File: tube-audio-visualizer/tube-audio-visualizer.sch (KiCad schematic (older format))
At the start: 19 parts, among them T1 EM80, U1 LM741, U2 LM386

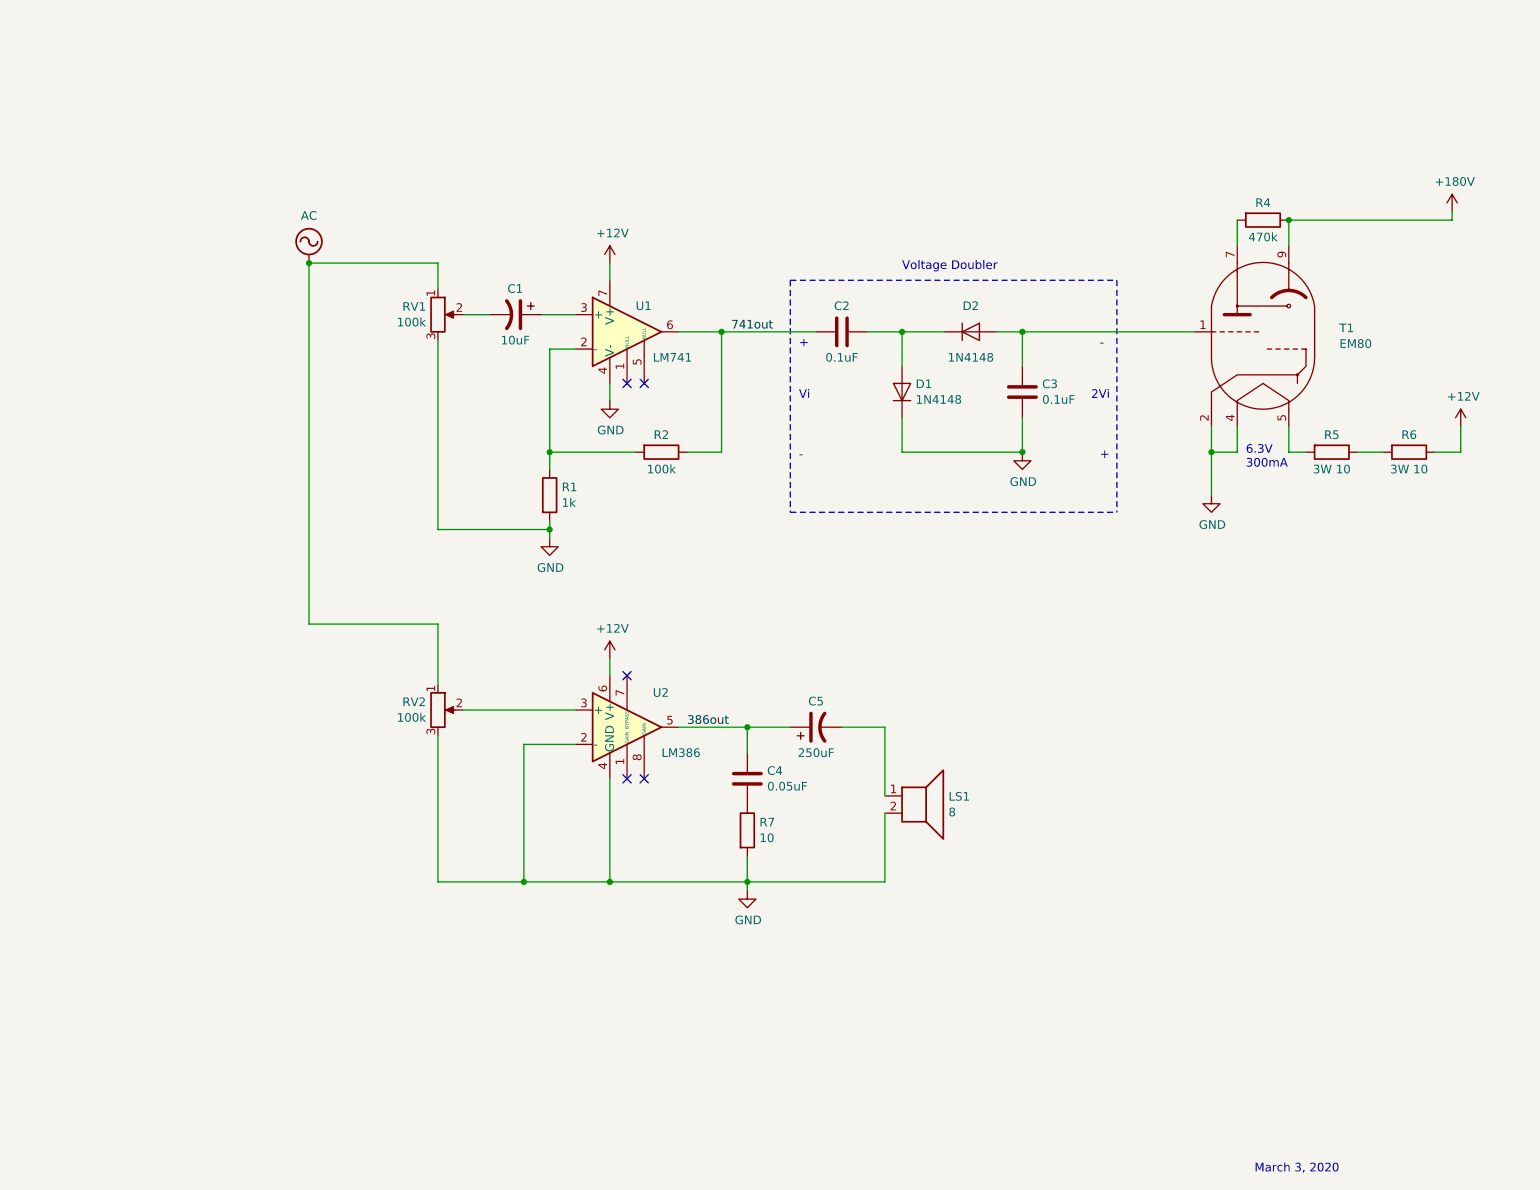
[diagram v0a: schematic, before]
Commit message: Added barrel jack to schematic. Connected 3.5mm female connector. Created footprint for 3.5mm female connector. Added footprints to all schematic symbols.
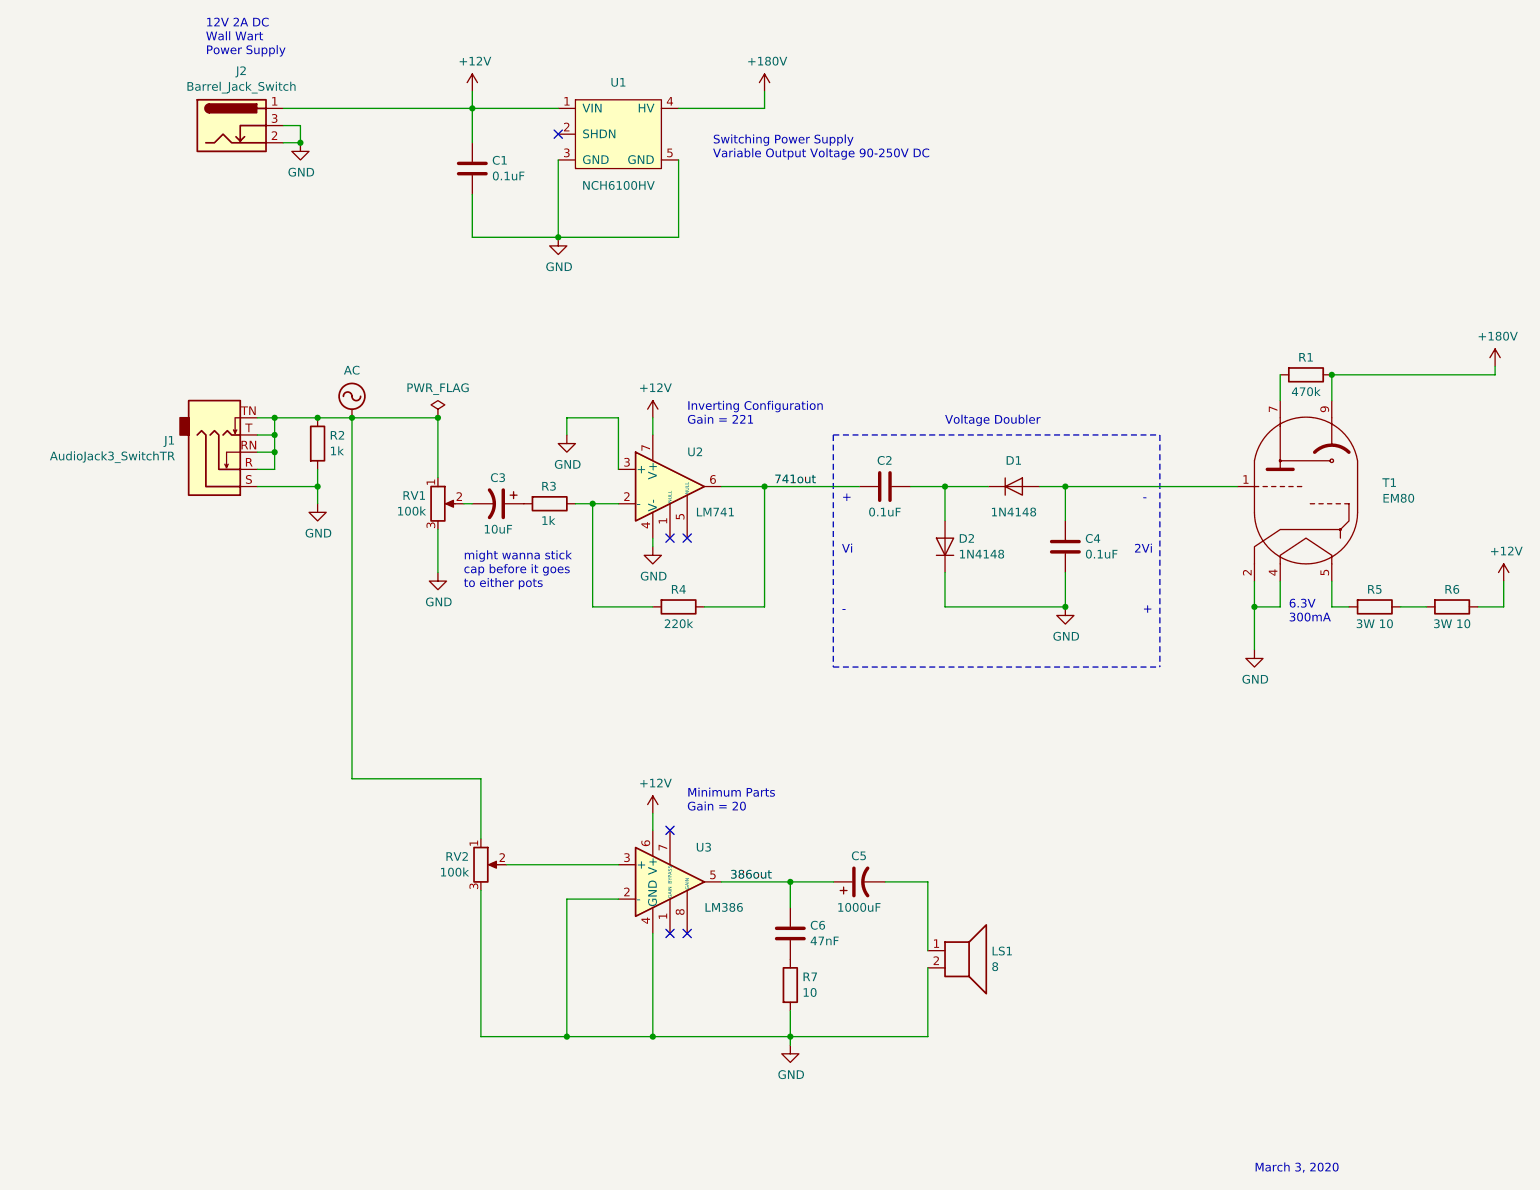
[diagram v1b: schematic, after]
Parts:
- added C1: 0.1uF, Capacitor_THT:C_Disc_D5.0mm_W2.5mm_P5.00mm, symbol Device:C
- added J1: AudioJack3_SwitchTR, footprints-nad:AudioJack_3_5_mm_Female, symbol Connector:AudioJack3_SwitchTR
- added J2: Barrel_Jack_Switch, Connector_BarrelJack:BarrelJack_CUI_PJ-102AH_Horizontal, symbol Connector:Barrel_Jack_Switch
- added R2: 1k, Resistor_THT:R_Axial_DIN0207_L6.3mm_D2.5mm_P10.16mm_Horizontal, symbol Device:R
- added U1: NCH6100HV, footprints-nad:NCH6100HV_PinSockets, symbol tube-audio-visualizer-rescue:NCH6100HV-symbols-nad
- C2: footprint (none) -> Capacitor_THT:C_Disc_D5.0mm_W2.5mm_P5.00mm
- C3: renamed from C1; footprint (none) -> Capacitor_THT:CP_Radial_D5.0mm_P2.00mm
- C4: renamed from C3; footprint (none) -> Capacitor_THT:C_Disc_D5.0mm_W2.5mm_P5.00mm
- C5: value 250uF -> 1000uF; footprint (none) -> Capacitor_THT:CP_Radial_D8.0mm_P3.50mm
- C6: renamed from C4; value 0.05uF -> 47nF; footprint (none) -> Capacitor_THT:C_Disc_D3.0mm_W2.0mm_P2.50mm
- D1: renamed from D2; footprint (none) -> Diode_THT:D_DO-35_SOD27_P7.62mm_Horizontal
- D2: renamed from D1; footprint (none) -> Diode_THT:D_DO-35_SOD27_P7.62mm_Horizontal
- LS1: footprint (none) -> Connector_PinSocket_2.54mm:PinSocket_1x02_P2.54mm_Vertical
- R4: renamed from R2; value 100k -> 220k
- R5, R6: footprint (none) -> Resistor_THT:R_Axial_DIN0516_L15.5mm_D5.0mm_P20.32mm_Horizontal
- RV1, RV2: footprint (none) -> Potentiometer_THT:Potentiometer_Bourns_3386P_Vertical
- renumbered R4 to R1, R1 to R3, U1 to U2, U2 to U3
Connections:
- net +12V: now also C1.1, J2.1, U1.1 (VIN)
- net +180V: now also U1.4 (HV)
- net AC: now also J1.R, J1.RN, J1.T, J1.TN, R2.1
- net GND: now also U2.3 (+), C1.2, J1.S, J2.2, J2.3, R2.2, U1.3 (GND), U1.5 (GND); no longer R3.2
- net at C3.1: now also R3.2; no longer U2.3 (+)
- no-connect marks 5 -> 6
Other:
- note added: "12V 2A DC\nWall Wart \nPower Supply"
- note added: "Inverting Configuration\nGain = 221"
- note added: "Minimum Parts\nGain = 20"
- note added: "Switching Power Supply\nVariable Output Voltage 90-250V DC"
- note added: "might wanna stick \ncap before it goes \nto either pots"
- moved on the sheet: C2, C3, C4, C5, C6, D1, D2, LS1, R1, R3, R4, R5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

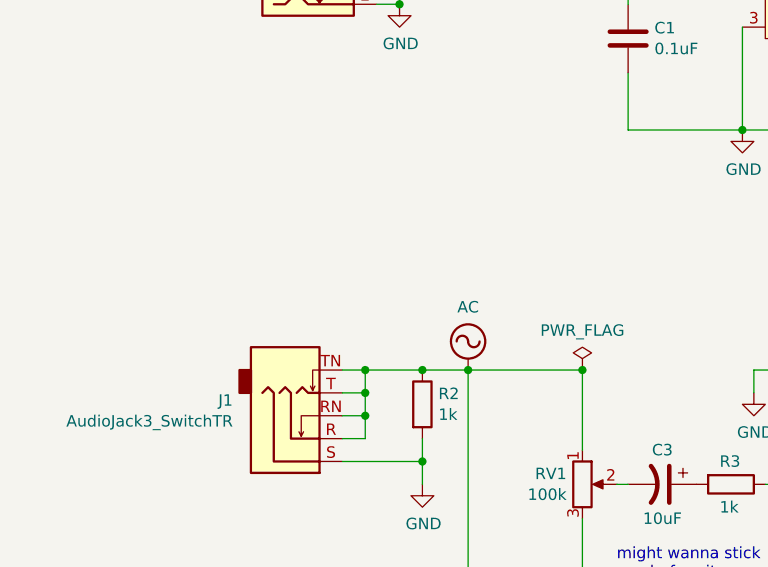
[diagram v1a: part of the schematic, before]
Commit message: Initial schematic to pcb update and parts grouped.
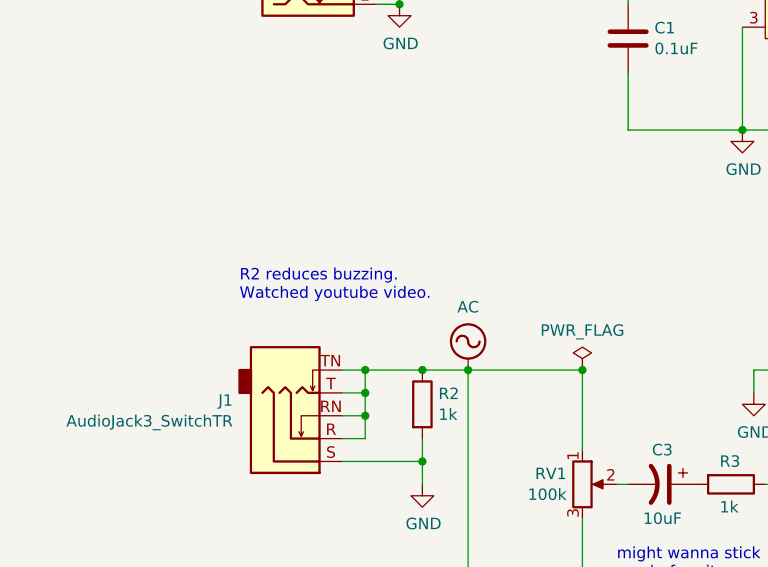
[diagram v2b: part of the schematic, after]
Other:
- note added: "R2 reduces buzzing.\nWatched youtube video."
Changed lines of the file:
@@
 Text Notes 2050 1150 0    50   ~ 0
 12V 2A DC\nWall Wart \nPower Supply
+Text Notes 1900 2950 0    50   ~ 0
+R2 reduces buzzing.\nWatched youtube video.
 $EndSCHEMATC

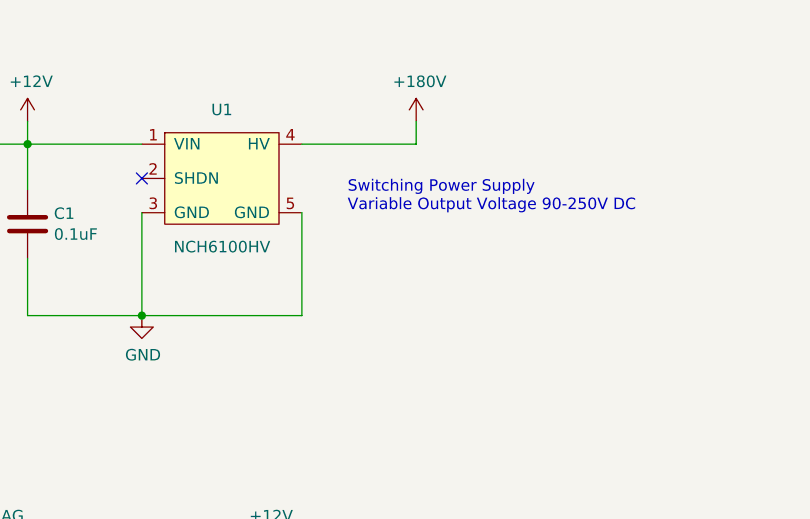
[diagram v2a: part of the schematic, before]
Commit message: Tube audio visualizer ready to be sent to fab. Added hot surface warning symbol footprint.
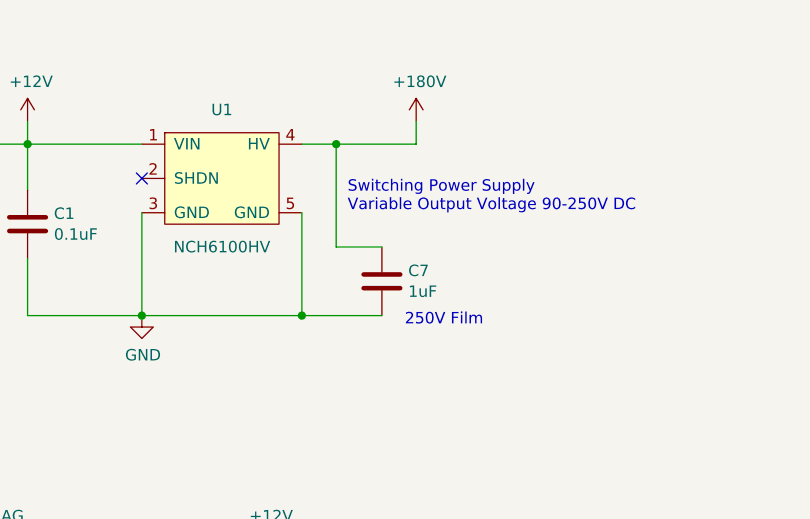
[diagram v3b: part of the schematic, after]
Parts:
- added C7: 1uF, footprints-nad:Cap_Film_250V_1uF_Nichicon, symbol Device:C
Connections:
- net +180V: now also C7.1
- net GND: now also C7.2
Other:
- note added: "250V Film"
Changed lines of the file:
@@
 	3600 1450 4100 1450
 Wire Wire Line
-	4800 1450 5300 1450
+	4800 1450 4950 1450
 Wire Wire Line
 	5300 1450 5300 1350
@@
 Text Notes 1900 2950 0    50   ~ 0
 R2 reduces buzzing.\nWatched youtube video.
+$Comp
+L Device:C C7
+U 1 1 5F6736A3
+P 5150 2050
+F 0 "C7" H 5265 2096 50  0000 L CNN
+F 1 "1uF" H 5265 2005 50  0000 L CNN
+F 2 "footprints-nad:Cap_Film_250V_1uF_Nichicon" H 5188 1900 50  0001 C CNN
+F 3 "~" H 5150 2050 50  0001 C CNN
+	1    5150 2050
+	1    0    0    -1
+$EndComp
+Wire Wire Line
+	5150 1900 4950 1900
+Wire Wire Line
+	4950 1900 4950 1450
+Connection ~ 4950 1450
+Wire Wire Line
+	4950 1450 5300 1450
+Wire Wire Line
+	5150 2200 4800 2200
+Connection ~ 4800 2200
+Text Notes 5250 2250 0    50   ~ 0
+250V Film
 $EndSCHEMATC
